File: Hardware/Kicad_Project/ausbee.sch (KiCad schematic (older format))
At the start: 0 parts

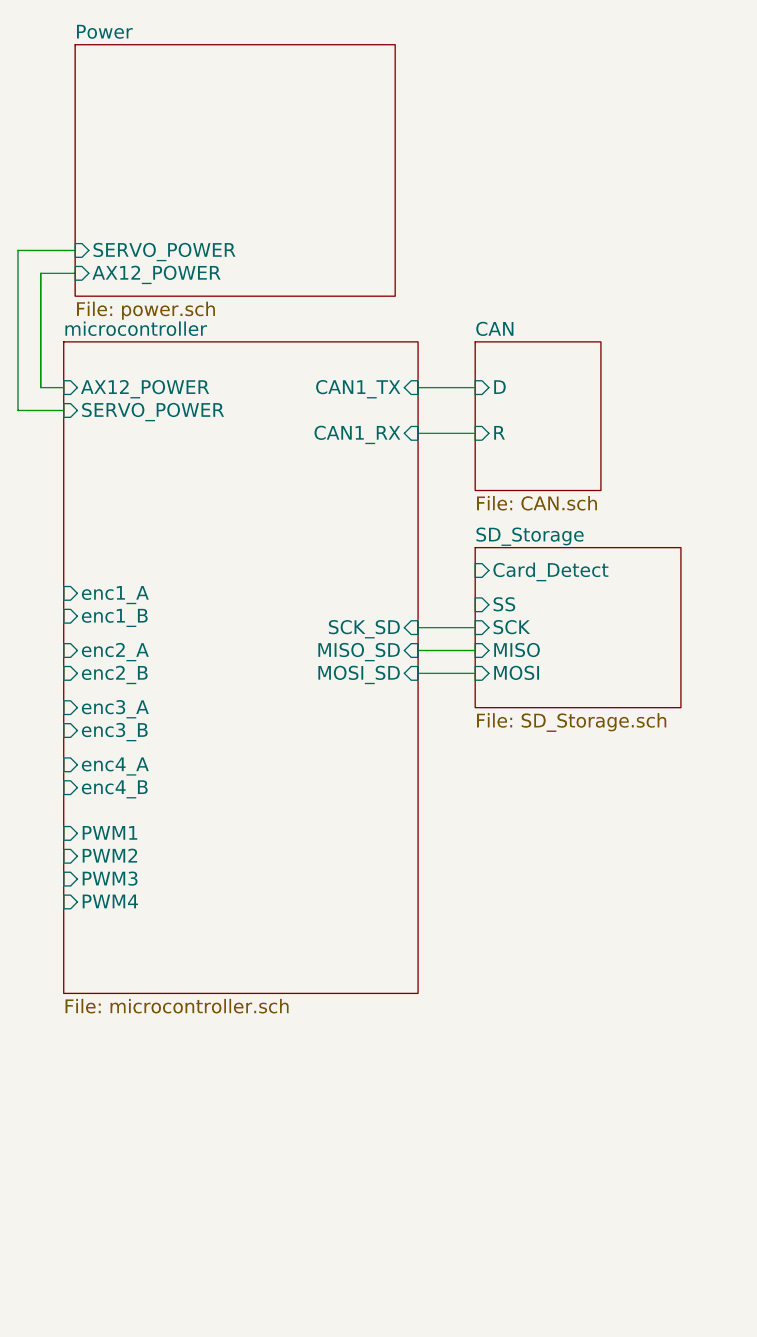
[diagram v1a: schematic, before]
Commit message: [HARDWARE] Add motor control signals around STM32
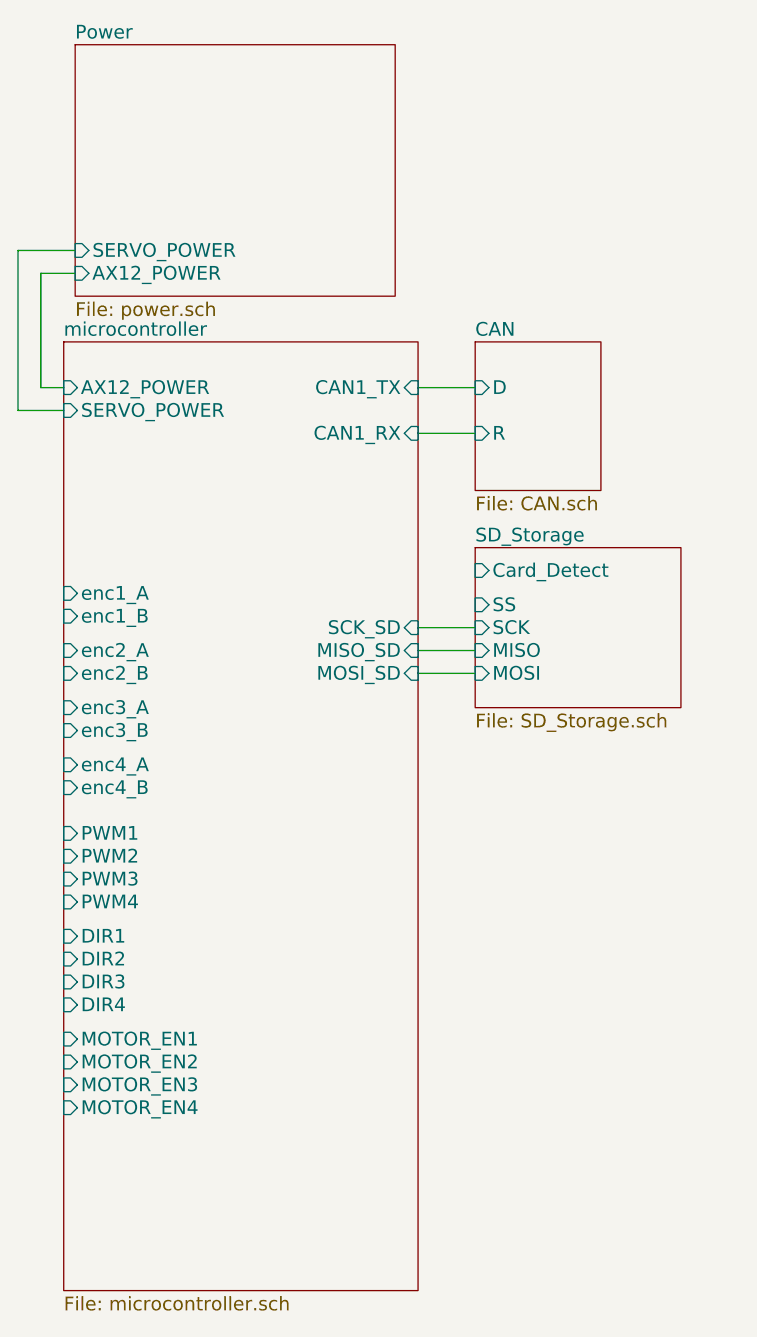
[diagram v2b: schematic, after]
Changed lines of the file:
@@
-EESchema Schematic File Version 2  date mar. 08 oct. 2013 19:33:19 CEST
+EESchema Schematic File Version 2  date mar. 08 oct. 2013 19:41:25 CEST
 LIBS:power
 LIBS:device
@@
 Comment4 ""
 $EndDescr
+$Sheet
+S 4250 2150 1550 4150
+U 52002A3D
+F0 "microcontroller" 60
+F1 "microcontroller.sch" 60
+F2 "CAN1_TX" I R 5800 2350 60
+F3 "CAN1_RX" I R 5800 2550 60
+F4 "enc4_B" I L 4250 4100 60
+F5 "enc4_A" I L 4250 4000 60
+F6 "enc3_B" I L 4250 3850 60
+F7 "enc3_A" I L 4250 3750 60
+F8 "enc2_B" I L 4250 3600 60
+F9 "enc2_A" I L 4250 3500 60
+F10 "enc1_B" I L 4250 3350 60
+F11 "enc1_A" I L 4250 3250 60
+F12 "PWM4" I L 4250 4600 60
+F13 "PWM3" I L 4250 4500 60
+F14 "PWM2" I L 4250 4400 60
+F15 "PWM1" I L 4250 4300 60
+F16 "AX12_POWER" I L 4250 2350 60
+F17 "SCK_SD" I R 5800 3400 60
+F18 "MOSI_SD" I R 5800 3600 60
+F19 "MISO_SD" I R 5800 3500 60
+F20 "SERVO_POWER" I L 4250 2450 60
+F21 "MOTOR_EN4" I L 4250 5500 60
+F22 "MOTOR_EN3" I L 4250 5400 60
+F23 "DIR4" I L 4250 5050 60
+F24 "DIR3" I L 4250 4950 60
+F25 "MOTOR_EN2" I L 4250 5300 60
+F26 "MOTOR_EN1" I L 4250 5200 60
+F27 "DIR2" I L 4250 4850 60
+F28 "DIR1" I L 4250 4750 60
+$EndSheet
 Wire Wire Line
 	4250 2450 4050 2450
@@
 F3 "D" I L 6050 2350 60
 $EndSheet
-$Sheet
-S 4250 2150 1550 2850
-U 52002A3D
-F0 "microcontroller" 60
-F1 "microcontroller.sch" 60
-F2 "CAN1_TX" I R 5800 2350 60
-F3 "CAN1_RX" I R 5800 2550 60
-F4 "enc4_B" I L 4250 4100 60
-F5 "enc4_A" I L 4250 4000 60
-F6 "enc3_B" I L 4250 3850 60
-F7 "enc3_A" I L 4250 3750 60
-F8 "enc2_B" I L 4250 3600 60
-F9 "enc2_A" I L 4250 3500 60
-F10 "enc1_B" I L 4250 3350 60
-F11 "enc1_A" I L 4250 3250 60
-F12 "PWM4" I L 4250 4600 60
-F13 "PWM3" I L 4250 4500 60
-F14 "PWM2" I L 4250 4400 60
-F15 "PWM1" I L 4250 4300 60
-F16 "AX12_POWER" I L 4250 2350 60
-F17 "SCK_SD" I R 5800 3400 60
-F18 "MOSI_SD" I R 5800 3600 60
-F19 "MISO_SD" I R 5800 3500 60
-F20 "SERVO_POWER" I L 4250 2450 60
-$EndSheet
 $EndSCHEMATC

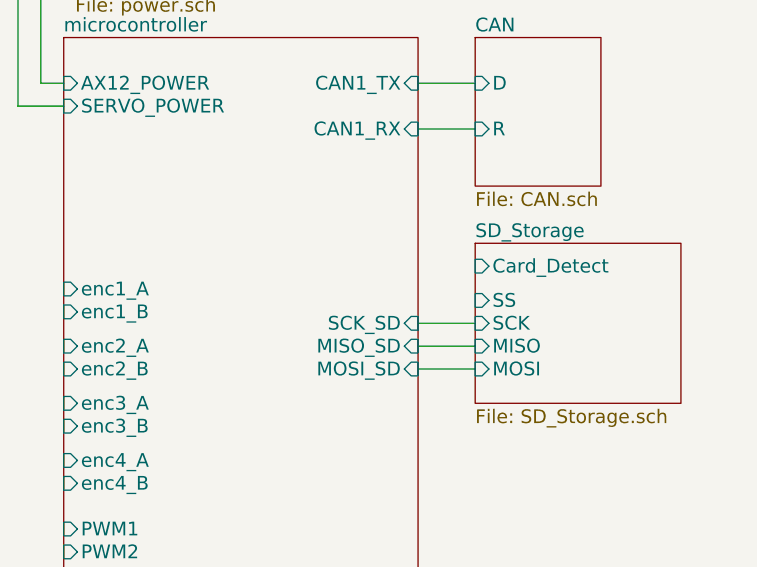
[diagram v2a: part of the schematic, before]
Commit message: [HARDWARE] Finalize SD interface
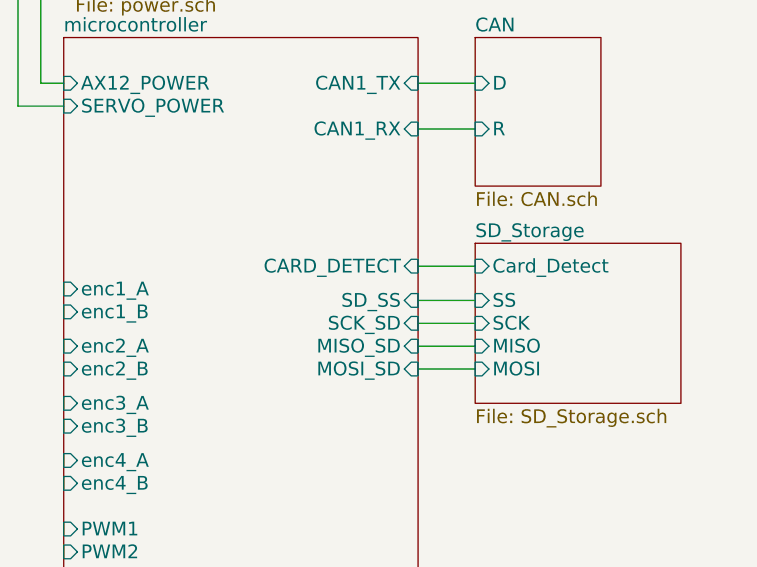
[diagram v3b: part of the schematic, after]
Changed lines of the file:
@@
-EESchema Schematic File Version 2  date mar. 08 oct. 2013 19:41:25 CEST
+EESchema Schematic File Version 2  date mar. 08 oct. 2013 19:56:47 CEST
 LIBS:power
 LIBS:device
@@
 Comment4 ""
 $EndDescr
+Wire Wire Line
+	6050 3300 5800 3300
+Wire Wire Line
+	4250 2450 4050 2450
+Wire Wire Line
+	4050 2450 4050 1750
+Wire Wire Line
+	4050 1750 4300 1750
+Wire Wire Line
+	5800 3500 6050 3500
+Wire Wire Line
+	4250 2350 4150 2350
+Wire Wire Line
+	4150 2350 4150 1850
+Wire Wire Line
+	4150 1850 4300 1850
+Wire Wire Line
+	6050 2550 5800 2550
+Wire Wire Line
+	6050 2350 5800 2350
+Wire Wire Line
+	6050 3400 5800 3400
+Wire Wire Line
+	6050 3600 5800 3600
+Wire Wire Line
+	5800 3150 6050 3150
 $Sheet
 S 4250 2150 1550 4150
@@
 F27 "DIR2" I L 4250 4850 60
 F28 "DIR1" I L 4250 4750 60
+F29 "CARD_DETECT" I R 5800 3150 60
+F30 "SD_SS" I R 5800 3300 60
 $EndSheet
-Wire Wire Line
-	4250 2450 4050 2450
-Wire Wire Line
-	4050 2450 4050 1750
-Wire Wire Line
-	4050 1750 4300 1750
-Wire Wire Line
-	5800 3500 6050 3500
-Wire Wire Line
-	4250 2350 4150 2350
-Wire Wire Line
-	4150 2350 4150 1850
-Wire Wire Line
-	4150 1850 4300 1850
-Wire Wire Line
-	6050 2550 5800 2550
-Wire Wire Line
-	6050 2350 5800 2350
-Wire Wire Line
-	6050 3400 5800 3400
-Wire Wire Line
-	6050 3600 5800 3600
 $Sheet
 S 4300 850  1400 1100
